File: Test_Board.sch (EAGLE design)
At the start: 33 parts, among them Q1 MOSFET_PCH-NDS8434, U1 Value, U2 Value

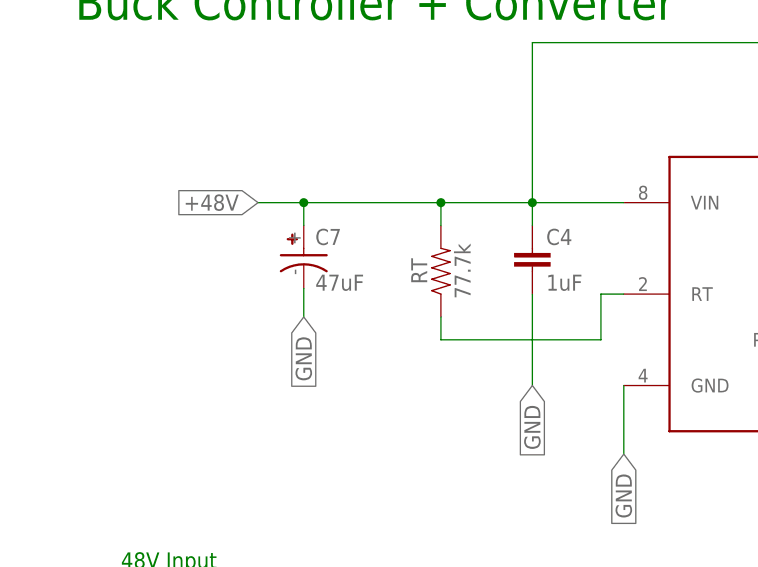
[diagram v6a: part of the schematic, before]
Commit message: couple silkscreen changes to order
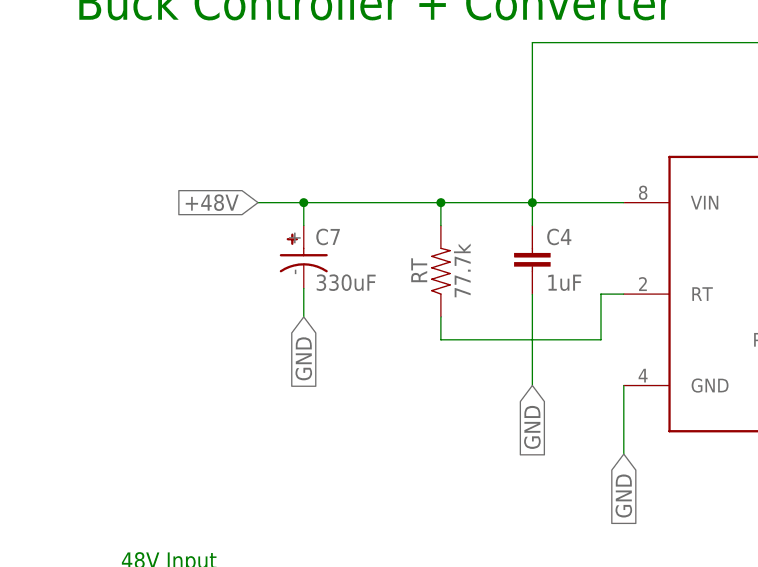
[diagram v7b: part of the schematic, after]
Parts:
- C7: value 47uF -> 330uF
- U1, U2: device Dist_OR_Controller:DIST_OR_DIODE -> Dist_OR_Controller:DIST_OR_DIODEDGK0008A_M
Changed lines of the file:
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@@
 <parts>
 <part name="FRAME1" library="frames" library_urn="urn:adsk.eagle:library:229" deviceset="A4L-LOC" device=""/>
-<part name="U1" library="Dist_OR_Controller" deviceset="DIST_OR_DIODE" device="" value="Value"/>
-<part name="U2" library="Dist_OR_Controller" deviceset="DIST_OR_DIODE" device="" value="Value"/>
+<part name="U1" library="Dist_OR_Controller" deviceset="DIST_OR_DIODE" device="DGK0008A_M" value="Value"/>
+<part name="U2" library="Dist_OR_Controller" deviceset="DIST_OR_DIODE" device="DGK0008A_M" value="Value"/>
 <part name="U$1" library="Reverse_Voltage_NMOS" deviceset="IRF1018EPBF" device=""/>
 <part name="U$2" library="Reverse_Voltage_NMOS" deviceset="IRF1018EPBF" device=""/>
@@
 <part name="RFB2" library="SparkFun-Resistors" library_urn="urn:adsk.eagle:library:532" deviceset="RESISTOR" device="0603" package3d_urn="urn:adsk.eagle:package:39650/1" value="10k"/>
 <part name="R3" library="SparkFun-Resistors" library_urn="urn:adsk.eagle:library:532" deviceset="RESISTOR" device="0603" package3d_urn="urn:adsk.eagle:package:39650/1" value="9.1k"/>
-<part name="C7" library="brick-capacitor-UCM1H331MNL1GS" deviceset="UCM1H331MNL1GS" device="" package3d_urn="urn:adsk.eagle:package:24202090/2" value="47uF"/>
+<part name="C7" library="brick-capacitor-UCM1H331MNL1GS" deviceset="UCM1H331MNL1GS" device="" package3d_urn="urn:adsk.eagle:package:24202090/2" value="330uF"/>
 <part name="C8" library="SparkFun-Capacitors" library_urn="urn:adsk.eagle:library:510" deviceset="0.1UF" device="-0603-25V-5%" package3d_urn="urn:adsk.eagle:package:37414/1" value="0.47uF"/>
 <part name="C9" library="SparkFun-Capacitors" library_urn="urn:adsk.eagle:library:510" deviceset="0.1UF" device="-0603-25V-5%" package3d_urn="urn:adsk.eagle:package:37414/1" value="1000pF"/>
